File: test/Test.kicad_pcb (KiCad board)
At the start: 2 copper layers, 49.8 x 63 mm, 15 parts, among them J1 Raspberry_Pi_2_3, J2 Power, J3 HDMI board, J4 Fan, J5 CNC, J6 IDC16, J7 UVPanel, J8 Pro Power, J9 Buzzer, Q1 BD139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

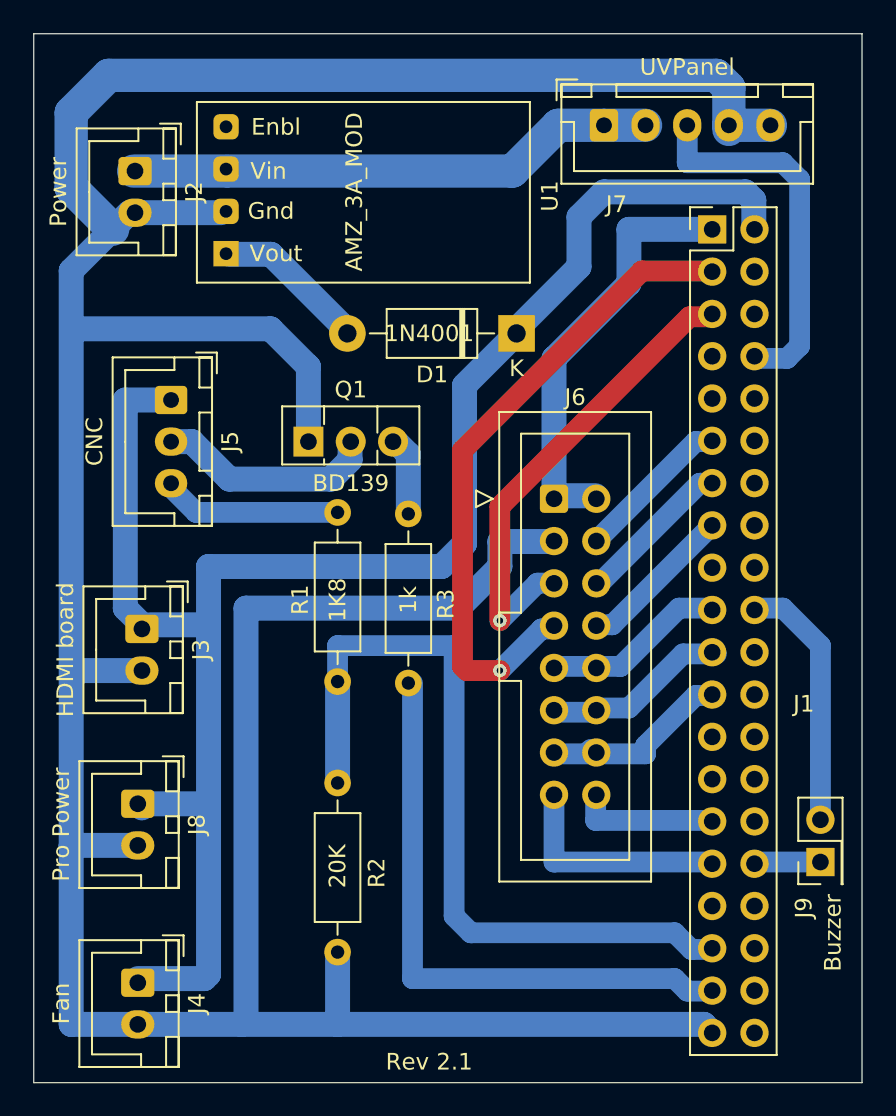
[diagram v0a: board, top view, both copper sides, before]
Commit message: Do not use pcb2gcode tool change gcode
pcb2gcode generates tool change code. Remove that at runtime, as the mill is already prepped.
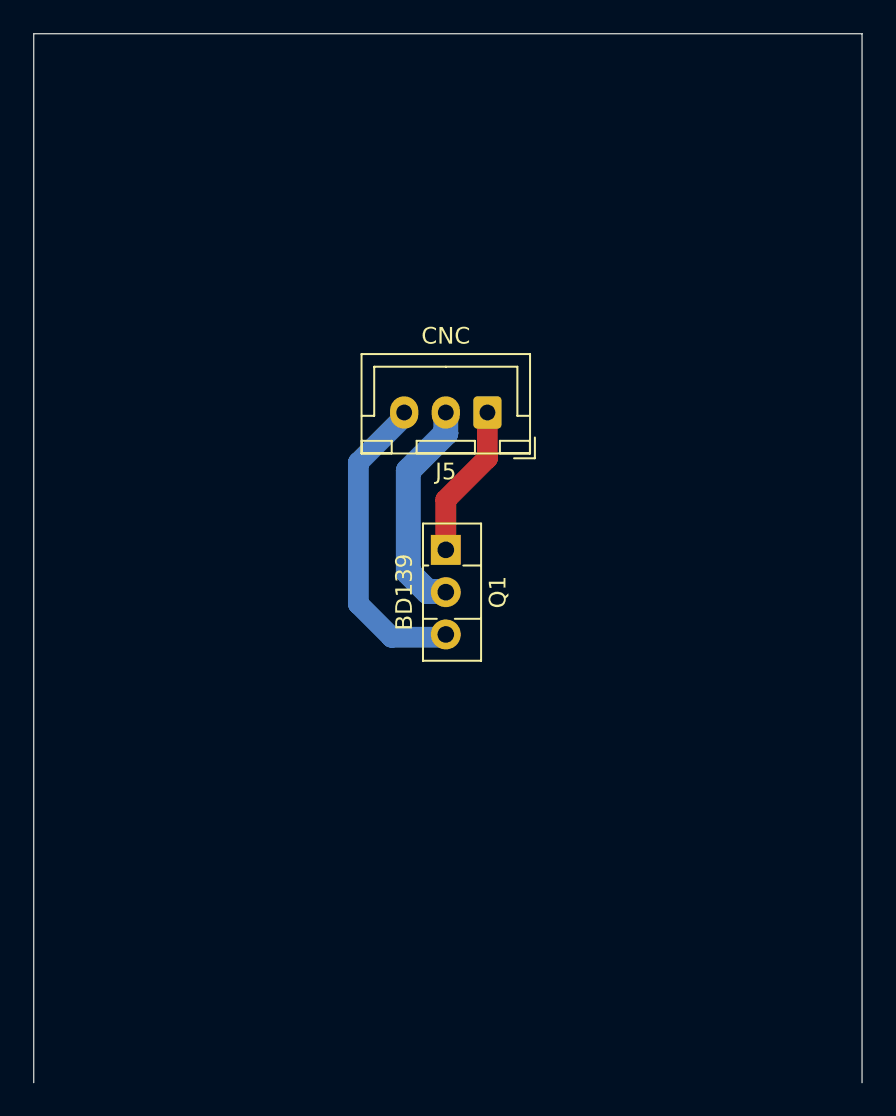
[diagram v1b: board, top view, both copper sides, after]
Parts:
- removed D1: 1N4001, Diode_THT:D_DO-41_SOD81_P10.16mm_Horizontal
- removed J1: Raspberry_Pi_2_3, pcb_etcher:PinSocket_2x20_P2.54mm_BacksideMount
- removed J2: Power, Connector_JST:JST_XH_B2B-XH-A_1x02_P2.50mm_Vertical
- removed J3: HDMI board, Connector_JST:JST_XH_B2B-XH-A_1x02_P2.50mm_Vertical
- removed J4: Fan, Connector_JST:JST_XH_B2B-XH-A_1x02_P2.50mm_Vertical
- removed J6: IDC16, Connector_IDC:IDC-Header_2x08_P2.54mm_Vertical
- removed J7: UVPanel, Connector_JST:JST_XH_B5B-XH-A_1x05_P2.50mm_Vertical
- removed J8: Pro Power, Connector_JST:JST_XH_B2B-XH-A_1x02_P2.50mm_Vertical
- removed J9: Buzzer, Connector_PinHeader_2.54mm:PinHeader_2x01_P2.54mm_Vertical
- removed R1: 1K8, Resistor_THT:R_Axial_DIN0207_L6.3mm_D2.5mm_P10.16mm_Horizontal
- removed R2: 20K, Resistor_THT:R_Axial_DIN0207_L6.3mm_D2.5mm_P10.16mm_Horizontal
- removed R3: 1k, Resistor_THT:R_Axial_DIN0207_L6.3mm_D2.5mm_P10.16mm_Horizontal
- removed U1: AMZ_3A_MOD, jkoz_custom:Amazon_3A_Power_Module
- moved J5 19.0 mm to (37.4, 31.9), turned to 180 degrees
- moved Q1 10.5 mm to (34.9, 40.1), turned to 270 degrees
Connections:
- J5 pad 3: ZProbeIn -> LaserControl
- Q1 pad 1: GND -> +5V
- Q1 pad 3: Net-(Q1-Pad3) -> LaserControl
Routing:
- net GND: track 240.8 -> 0.00 mm
- net +5V: track 105.6 -> 9.04 mm
- net ZProbe3V3: track 47.8 -> 0.00 mm
- net SDA: track 38.8 -> 0.00 mm, vias 1 -> 0
- net +24V: track 31.6 -> 0.00 mm
- net SCL: track 28.0 -> 0.00 mm, vias 1 -> 0
- net +3V3: track 25.4 -> 0.00 mm
- net UVControl: track 22.5 -> 0.00 mm
- net LaserControl: track 36.1 -> 18.2 mm
- net T_CS: track 13.0 -> 0.00 mm
- net SLCK: track 11.5 -> 0.00 mm
- net MOSI: track 11.2 -> 0.00 mm
- net MISO: track 11.2 -> 0.00 mm
- net ZProbeIn: track 10.6 -> 0.00 mm
- net CS: track 9.76 -> 0.00 mm
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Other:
- board text removed: "Rev 2.1"
